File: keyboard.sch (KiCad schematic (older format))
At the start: 106 parts, among them J1 USB_mini_micro_B, U1 ATMEGA32U4

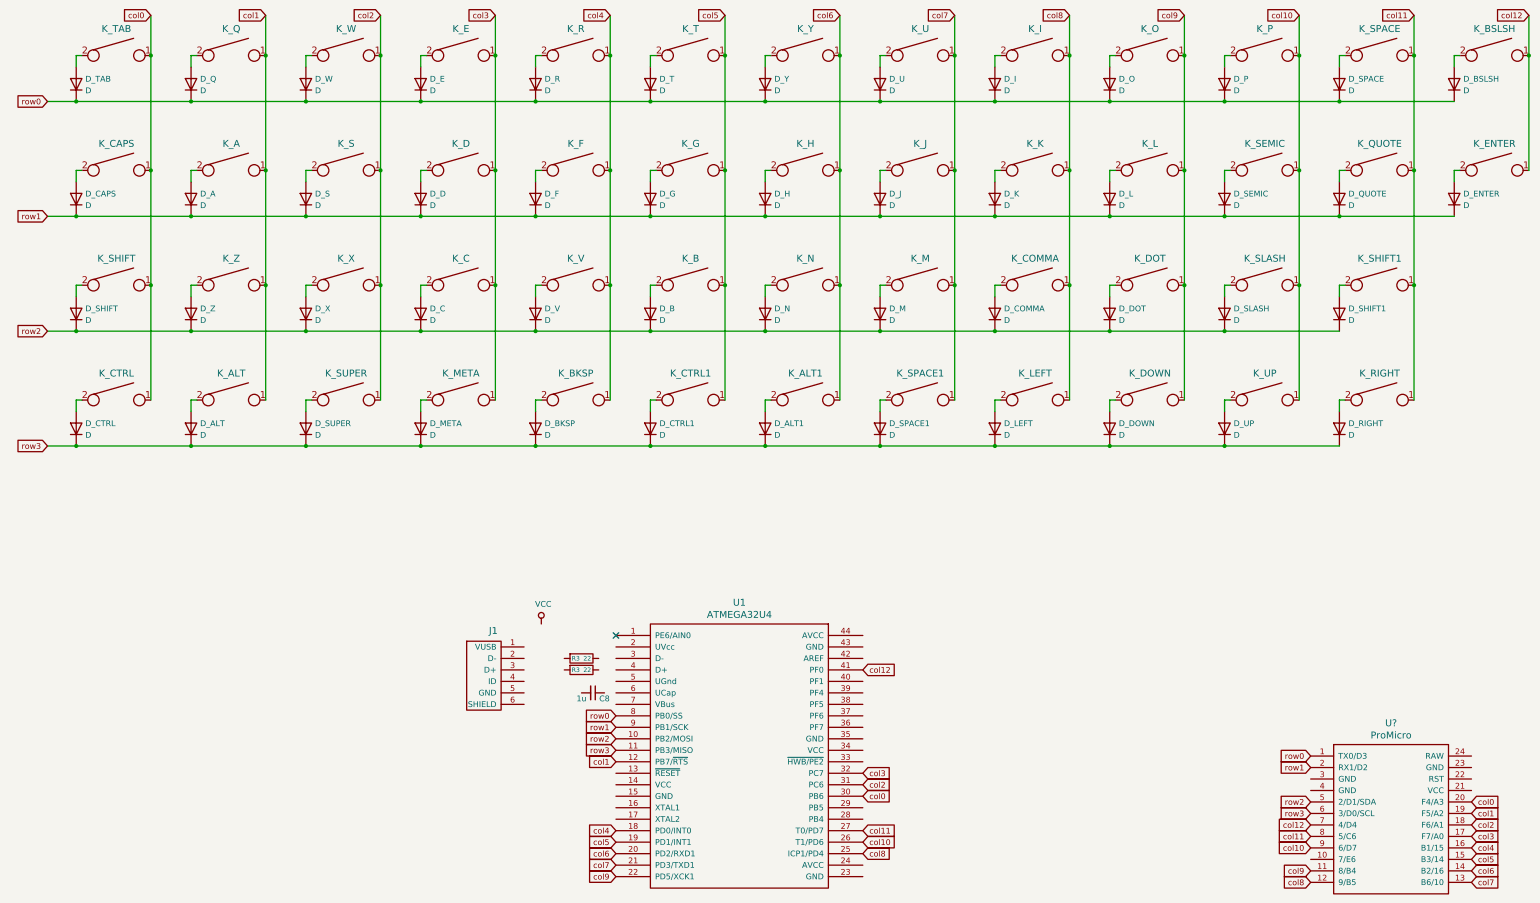
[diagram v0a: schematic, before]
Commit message: removed atmega and updated schematic with promicro
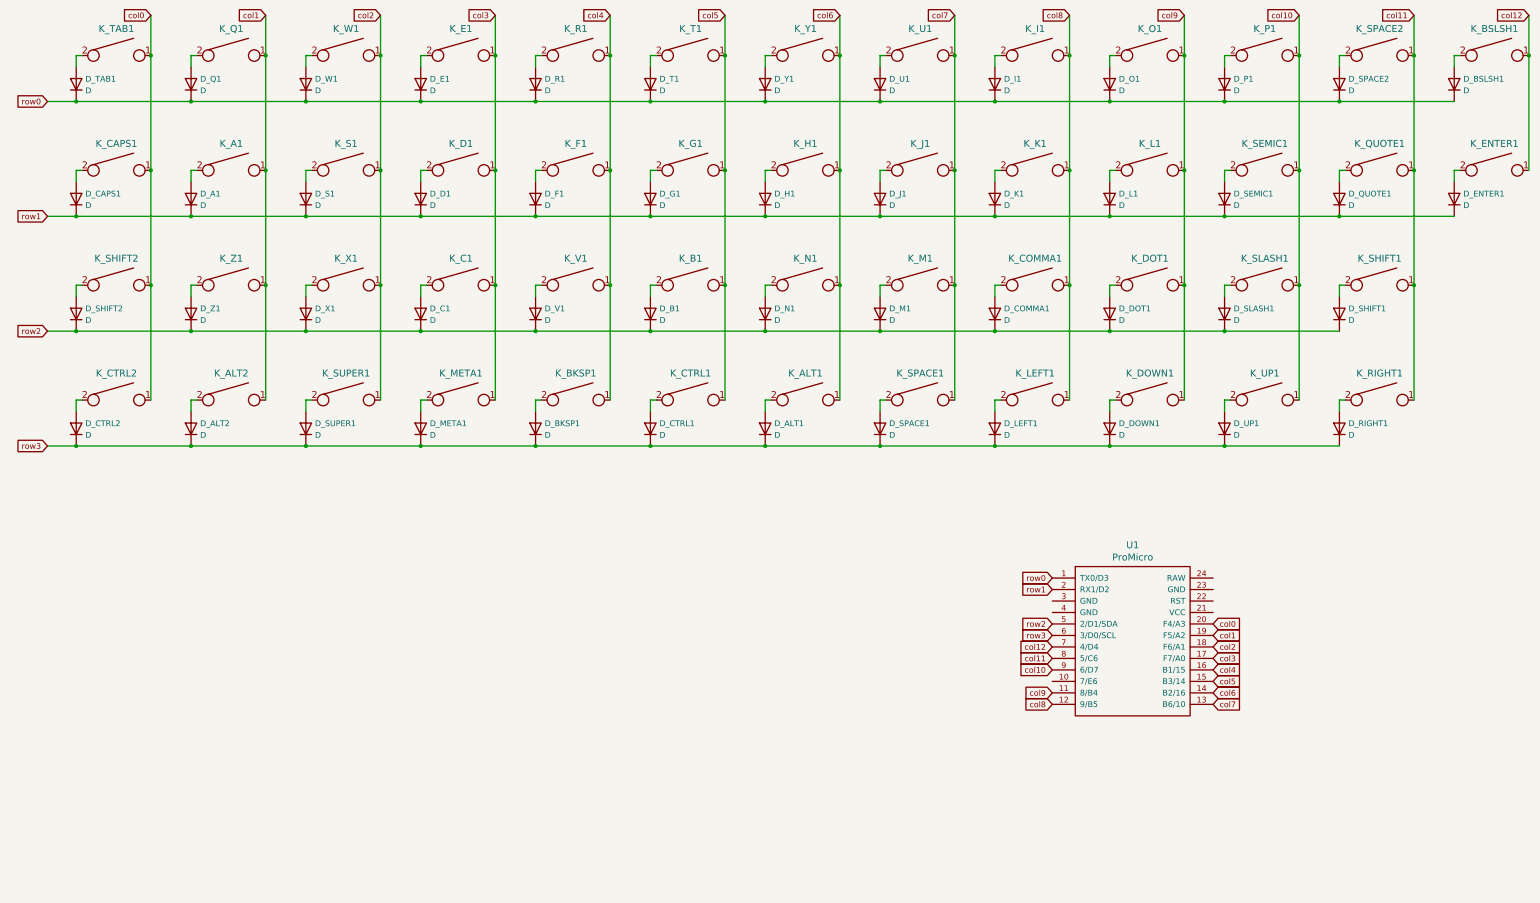
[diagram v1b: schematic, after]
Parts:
- removed C8: 1u, Capacitor_SMD:C_0805_2012Metric_Pad1.15x1.40mm_HandSolder, symbol Device:C_Small
- removed D_E: D, keyboard_parts:D_SOD123_axial, symbol Device:D
- removed J1: USB_mini_micro_B, keyboard_parts:USB_miniB_hirose_5S8, symbol keyboard_parts:USB_mini_micro_B
- removed R3 (x2): 22, Resistor_SMD:R_0805_2012Metric_Pad1.15x1.40mm_HandSolder, symbol Device:R
- removed U1: ATMEGA32U4, Package_QFP:TQFP-44_10x10mm_P0.8mm, symbol keyboard_parts:ATMEGA32U4
- added D_E1: D, keyboard_parts:D_SOD123_axial, symbol Device:D
- gave numbers to parts that had none: 1
- renumbered D_A to D_A1, D_ALT to D_ALT2, D_B to D_B1, D_BKSP to D_BKSP1, D_BSLSH to D_BSLSH1, D_C to D_C1, D_CAPS to D_CAPS1, D_COMMA to D_COMMA1, D_CTRL to D_CTRL2, D_D to D_D1, D_DOT to D_DOT1, D_DOWN to D_DOWN1, D_ENTER to D_ENTER1, D_F to D_F1, D_G to D_G1, D_H to D_H1, D_I to D_I1, D_J to D_J1, D_K to D_K1, D_L to D_L1, D_LEFT to D_LEFT1, D_M to D_M1, D_META to D_META1, D_N to D_N1, D_O to D_O1, D_P to D_P1, D_Q to D_Q1, D_QUOTE to D_QUOTE1, D_R to D_R1, D_RIGHT to D_RIGHT1, D_S to D_S1, D_SEMIC to D_SEMIC1, D_SHIFT to D_SHIFT2, D_SLASH to D_SLASH1, D_SPACE to D_SPACE2, D_SUPER to D_SUPER1, D_T to D_T1, D_TAB to D_TAB1, D_U to D_U1, D_UP to D_UP1, D_V to D_V1, D_W to D_W1, D_X to D_X1, D_Y to D_Y1, D_Z to D_Z1, K_A to K_A1, K_ALT to K_ALT2, K_B to K_B1, K_BKSP to K_BKSP1, K_BSLSH to K_BSLSH1, K_C to K_C1, K_CAPS to K_CAPS1, K_COMMA to K_COMMA1, K_CTRL to K_CTRL2, K_D to K_D1, K_DOT to K_DOT1, K_DOWN to K_DOWN1, K_E to K_E1, K_ENTER to K_ENTER1, K_F to K_F1, K_G to K_G1, K_H to K_H1, K_I to K_I1, K_J to K_J1, K_K to K_K1, K_L to K_L1, K_LEFT to K_LEFT1, K_M to K_M1, K_META to K_META1, K_N to K_N1, K_O to K_O1, K_P to K_P1, K_Q to K_Q1, K_QUOTE to K_QUOTE1, K_R to K_R1, K_RIGHT to K_RIGHT1, K_S to K_S1, K_SEMIC to K_SEMIC1, K_SHIFT to K_SHIFT2, K_SLASH to K_SLASH1, K_SPACE to K_SPACE2, K_SUPER to K_SUPER1, K_T to K_T1, K_TAB to K_TAB1, K_U to K_U1, K_UP to K_UP1, K_V to K_V1, K_W to K_W1, K_X to K_X1, K_Y to K_Y1, K_Z to K_Z1
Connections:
- net row0: now also D_E1.1 (K)
- net at K_E1.2: now also D_E1.2 (A)
- no-connect marks 1 -> 0
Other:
- moved on the sheet: U1

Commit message: aligned switches
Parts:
- K_A1, K_ALT2, K_B1, K_C1, K_COMMA1, K_D1, K_DOT1, K_DOWN1, K_E1, K_F1, K_G1, K_H1, K_I1, K_J1, K_K1, K_L1, K_LEFT1, K_M1, K_META1, K_N1, K_O1, K_P1, K_Q1, K_QUOTE1, K_R1, K_S1, K_SEMIC1, K_SLASH1, K_SPACE2, K_SUPER1, K_T1, K_U1, K_UP1, K_V1, K_W1, K_X1, K_Y1, K_Z1: footprint MX_Alps_Hybrid:MX-1U-NoLED -> MX_ALPS_Hybrid:MX-1U
- K_ALT1, K_CTRL1: footprint MX_Alps_Hybrid:MX-1U-NoLED -> MX_ALPS_Hybrid:MX-2U
- K_BKSP1, K_CTRL2, K_SPACE1: footprint MX_Alps_Hybrid:MX-1.25U-NoLED -> MX_ALPS_Hybrid:MX-1.25U
- K_BSLSH1, K_TAB1: footprint MX_Alps_Hybrid:MX-1.5U-NoLED -> MX_ALPS_Hybrid:MX-1.5U
- K_CAPS1: footprint MX_Alps_Hybrid:MX-1.75U-NoLED -> MX_ALPS_Hybrid:MX-1.75U
- K_ENTER1, K_SHIFT2: footprint MX_Alps_Hybrid:MX-2.25U-NoLED -> MX_ALPS_Hybrid:MX-2.25U
- K_RIGHT1: footprint MX_Alps_Hybrid:MX-1.25U-NoLED -> MX_ALPS_Hybrid:MX-1U
- K_SHIFT1: footprint MX_Alps_Hybrid:MX-2.75U-NoLED -> MX_ALPS_Hybrid:MX-2.75U
- U1: footprint (none) -> kbd:ProMicro_v3.5

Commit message: add reset switch and ground zones
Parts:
- added SW1: SW_PUSH, kbd:ResetSW, symbol keyboard_parts:SW_PUSH
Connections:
- net RESET: now reaches U1.22 (RST)
- net RESET: now also SW1.2
- net GND: now reaches U1.23 (GND)
- net GND: now also U1.3 (GND), U1.4 (GND), SW1.1
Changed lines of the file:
@@
 Text GLabel 9650 6150 0    50   Input ~ 0
 col12
+Wire Wire Line
+	9650 5850 9650 5750
+Text GLabel 11050 5750 2    50   Input ~ 0
+RESET
+Text GLabel 13300 5600 3    50   Input ~ 0
+RESET
+$Comp
+L keyboard_parts:SW_PUSH SW1
+U 1 1 6256CA71
+P 13000 5600
+F 0 "SW1" H 13000 5855 50  0000 C CNN
+F 1 "SW_PUSH" H 13000 5764 50  0000 C CNN
+F 2 "kbd:ResetSW" H 13000 5600 60  0001 C CNN
+F 3 "" H 13000 5600 60  0000 C CNN
+	1    13000 5600
+	1    0    0    -1
+$EndComp
+$Comp
+L power:GND #PWR?
+U 1 1 6267FC7D
+P 9350 5850
+F 0 "#PWR?" H 9350 5600 50  0001 C CNN
+F 1 "GND" V 9355 5722 50  0000 R CNN
+F 2 "" H 9350 5850 50  0001 C CNN
+F 3 "" H 9350 5850 50  0001 C CNN
+	1    9350 5850
+	0    1    1    0
+$EndComp
+Wire Wire Line
+	9350 5850 9650 5850
+Connection ~ 9650 5850
+$Comp
+L power:GND #PWR?
+U 1 1 62696D4D
+P 11350 5650
+F 0 "#PWR?" H 11350 5400 50  0001 C CNN
+F 1 "GND" V 11355 5522 50  0000 R CNN
+F 2 "" H 11350 5650 50  0001 C CNN
+F 3 "" H 11350 5650 50  0001 C CNN
+	1    11350 5650
+	0    -1   -1   0
+$EndComp
+Wire Wire Line
+	11050 5650 11350 5650
+$Comp
+L power:GND #PWR?
+U 1 1 626A2C50
+P 12700 5600
+F 0 "#PWR?" H 12700 5350 50  0001 C CNN
+F 1 "GND" H 12705 5427 50  0000 C CNN
+F 2 "" H 12700 5600 50  0001 C CNN
+F 3 "" H 12700 5600 50  0001 C CNN
+	1    12700 5600
+	1    0    0    -1
+$EndComp
 $EndSCHEMATC
